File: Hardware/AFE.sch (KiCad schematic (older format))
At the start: 43 parts, among them U5 4069, U801 MCP47CXBX2, Y1 MountPad3, Y2 MountPad3

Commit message: Checking in some libraries.
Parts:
- removed GROUND1: GND_PAD, GaudiLabsFootPrints:MountPad3, symbol OpenThereminCC-rescue:TEST_1P
- removed W1: FIDUCIAL1, Fiducials:Fiducial_1mm_Dia_2.54mm_Outer_CopperTop, symbol OpenThereminCC-rescue:TEST_1P
- removed W2: FIDUCIAL2, Fiducials:Fiducial_1mm_Dia_2.54mm_Outer_CopperTop, symbol OpenThereminCC-rescue:TEST_1P
- removed Y1, Y2: MountPad3, GaudiLabsFootPrints:MountPad3, symbol OpenThereminCC-rescue:MountPad3
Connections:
- net labels added: PitchAnt, VolAnt
- wire segments 125 -> 123
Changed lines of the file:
@@
-$EndComp
-$Comp
-L OpenThereminCC-rescue:MountPad3 Y1
-U 1 1 5712BCA3
-P 850 1800
-F 0 "Y1" H 744 1600 60  0000 C CNN
-F 1 "MountPad3" H 900 1850 60  0000 C CNN
-F 2 "GaudiLabsFootPrints:MountPad3" H 850 1800 60  0001 C CNN
-F 3 "" H 850 1800 60  0000 C CNN
-	1    850  1800
-	-1   0    0    1
 $EndComp
 $Comp
@@
 $EndComp
 $Comp
-L OpenThereminCC-rescue:MountPad3 Y2
-U 1 1 571F63BE
-P 850 5250
-F 0 "Y2" H 744 5050 60  0000 C CNN
-F 1 "MountPad3" H 900 5300 60  0000 C CNN
-F 2 "GaudiLabsFootPrints:MountPad3" H 850 5250 60  0001 C CNN
-F 3 "" H 850 5250 60  0000 C CNN
-	1    850  5250
-	-1   0    0    1
-$EndComp
-$Comp
 L OpenThereminCC-rescue:FILTER L2
 U 1 1 571F63C6
@@
 	3650 4900 3650 4550
 Wire Wire Line
-	850  5250 850  4250
-Wire Wire Line
 	1700 7000 2200 7000
 Wire Wire Line
@@
 	1    0    0    -1
 $EndComp
-Wire Wire Line
-	850  1800 850  800
-$Comp
-L OpenThereminCC-rescue:TEST_1P GROUND1
-U 1 1 5735D84B
-P 3000 7100
-F 0 "GROUND1" H 2950 7250 50  0000 R CNN
-F 1 "GND_PAD" H 3100 7400 50  0000 R CNN
-F 2 "GaudiLabsFootPrints:MountPad3" H 3200 7100 50  0001 C CNN
-F 3 "" H 3200 7100 50  0000 C CNN
-	1    3000 7100
-	1    0    0    -1
-$EndComp
-$Comp
-L power:GND #PWR011
-U 1 1 5735ECC6
-P 3000 7100
-F 0 "#PWR011" H 3000 6850 50  0001 C CNN
-F 1 "GND" H 3008 6927 50  0000 C CNN
-F 2 "" H 3000 7100 50  0000 C CNN
-F 3 "" H 3000 7100 50  0000 C CNN
-	1    3000 7100
-	1    0    0    -1
-$EndComp
 $Comp
 L power:VSS #PWR017
@@
 	2300 2400 2300 2350
 Connection ~ 2550 2400
-$Comp
-L OpenThereminCC-rescue:TEST_1P W1
-U 1 1 57DB2880
-P 5900 7600
-F 0 "W1" V 5800 7650 50  0000 C CNN
-F 1 "FIDUCIAL1" V 5900 8000 50  0000 C CNN
-F 2 "Fiducials:Fiducial_1mm_Dia_2.54mm_Outer_CopperTop" H 6100 7600 50  0001 C CNN
-F 3 "" H 6100 7600 50  0000 C CNN
-	1    5900 7600
-	0    -1   -1   0
-$EndComp
-$Comp
-L OpenThereminCC-rescue:TEST_1P W2
-U 1 1 57DB3B8D
-P 6100 7600
-F 0 "W2" V 6200 7650 50  0000 L CNN
-F 1 "FIDUCIAL2" V 6100 7900 50  0000 L CNN
-F 2 "Fiducials:Fiducial_1mm_Dia_2.54mm_Outer_CopperTop" H 6300 7600 50  0001 C CNN
-F 3 "" H 6300 7600 50  0000 C CNN
-	1    6100 7600
-	0    1    1    0
-$EndComp
 Wire Wire Line
 	2550 1100 2750 1100
@@
 	1    0    0    -1
 $EndComp
+Text HLabel 900  1800 0    50   UnSpc ~ 0
+PitchAnt
+Text HLabel 900  5250 0    50   UnSpc ~ 0
+VolAnt
 $EndSCHEMATC

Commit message: Moving some components around.
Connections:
- net labels added: DAC_Latch, DO_PITCH, DO_VOLUME, i2c0_SCL, i2c0_SDA
- net labels removed: DAC_LATCH
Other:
- note added: "Changed DAC to i2c"
- note removed: "Change DAC to i2c"
- note removed: "TEST POINTS!!"
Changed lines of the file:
@@
 Wire Wire Line
 	1700 3550 2400 3550
-Text GLabel 8600 4600 2    60   Input ~ 0
-DAC_LATCH
 $Comp
 L OpenThereminCC-rescue:C C20
@@
 VO_VOL
 Text Notes 8150 6350 0    197  ~ 0
-Change DAC to i2c
-Text Notes 4250 5450 0    197  ~ 0
-TEST POINTS!!
-Text Notes 4300 1850 0    197  ~ 0
-TEST POINTS!!
+Changed DAC to i2c
 Text Notes 2400 5900 0    197  ~ 0
 220pF?\n
@@
 Text HLabel 900  5250 0    50   UnSpc ~ 0
 VolAnt
+Text HLabel 4450 1800 2    50   Output ~ 0
+DO_PITCH
+Text HLabel 4200 5250 2    50   Output ~ 0
+DO_VOLUME
+Text HLabel 8650 4200 2    50   BiDi ~ 0
+i2c0_SDA
+Text HLabel 8650 4300 2    50   Input ~ 0
+i2c0_SCL
+Text HLabel 8650 4600 2    50   Input ~ 0
+DAC_Latch
 $EndSCHEMATC

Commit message: Cleaning up a few associations, changing 0805 to 0603 footprints on AFE.
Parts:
- C801: renamed from C5; footprint GaudiLabsFootPrints:0805G -> Capacitor_SMD:C_0603_1608Metric_Pad1.08x0.95mm_HandSolder; symbol OpenThereminCC-rescue:C -> Device:C
- C802: renamed from C6; footprint GaudiLabsFootPrints:0805G -> Capacitor_SMD:C_0603_1608Metric_Pad1.08x0.95mm_HandSolder; symbol OpenThereminCC-rescue:C -> Device:C
- C803: renamed from C12; footprint GaudiLabsFootPrints:0805G -> Capacitor_SMD:C_0603_1608Metric_Pad1.08x0.95mm_HandSolder; symbol OpenThereminCC-rescue:C -> Device:C
- C804: renamed from C13; footprint GaudiLabsFootPrints:0805G -> Capacitor_SMD:C_0603_1608Metric_Pad1.08x0.95mm_HandSolder; symbol OpenThereminCC-rescue:C -> Device:C
- C805: renamed from C4; footprint GaudiLabsFootPrints:0805G -> Capacitor_SMD:C_0603_1608Metric_Pad1.08x0.95mm_HandSolder; symbol OpenThereminCC-rescue:C -> Device:C
- C806: renamed from C11; footprint GaudiLabsFootPrints:0805G -> Capacitor_SMD:C_0603_1608Metric_Pad1.08x0.95mm_HandSolder; symbol OpenThereminCC-rescue:C -> Device:C
- C807: renamed from C2; footprint GaudiLabsFootPrints:0805G -> Capacitor_SMD:C_0603_1608Metric_Pad1.08x0.95mm_HandSolder; symbol OpenThereminCC-rescue:C -> Device:C
- C808: renamed from C3; footprint GaudiLabsFootPrints:0805G -> Capacitor_SMD:C_0603_1608Metric_Pad1.08x0.95mm_HandSolder; symbol OpenThereminCC-rescue:C -> Device:C
- C809: renamed from C9; footprint GaudiLabsFootPrints:0805G -> Capacitor_SMD:C_0603_1608Metric_Pad1.08x0.95mm_HandSolder; symbol OpenThereminCC-rescue:C -> Device:C
- C810: renamed from C10; footprint GaudiLabsFootPrints:0805G -> Capacitor_SMD:C_0603_1608Metric_Pad1.08x0.95mm_HandSolder; symbol OpenThereminCC-rescue:C -> Device:C
- C811: renamed from C7; footprint GaudiLabsFootPrints:0805G -> Capacitor_SMD:C_0603_1608Metric_Pad1.08x0.95mm_HandSolder; symbol OpenThereminCC-rescue:C -> Device:C
- C812: renamed from C14; footprint GaudiLabsFootPrints:0805G -> Capacitor_SMD:C_0603_1608Metric_Pad1.08x0.95mm_HandSolder; symbol OpenThereminCC-rescue:C -> Device:C
- C813: renamed from C1; footprint GaudiLabsFootPrints:0805G -> Capacitor_SMD:C_0603_1608Metric_Pad1.08x0.95mm_HandSolder; symbol OpenThereminCC-rescue:C -> Device:C
- C814: renamed from C8; footprint GaudiLabsFootPrints:0805G -> Capacitor_SMD:C_0603_1608Metric_Pad1.08x0.95mm_HandSolder; symbol OpenThereminCC-rescue:C -> Device:C
- C815: renamed from C23; footprint GaudiLabsFootPrints:0805G -> Capacitor_SMD:C_0603_1608Metric_Pad1.08x0.95mm_HandSolder; symbol OpenThereminCC-rescue:C -> Device:C
- C816: renamed from C24; footprint GaudiLabsFootPrints:0805G -> Capacitor_SMD:C_0603_1608Metric_Pad1.08x0.95mm_HandSolder; symbol OpenThereminCC-rescue:C -> Device:C
- C817: renamed from C25; footprint GaudiLabsFootPrints:0805G -> Capacitor_SMD:C_0603_1608Metric_Pad1.08x0.95mm_HandSolder; symbol OpenThereminCC-rescue:C -> Device:C
- C818: renamed from C26; footprint GaudiLabsFootPrints:0805G -> Capacitor_SMD:C_0603_1608Metric_Pad1.08x0.95mm_HandSolder; symbol OpenThereminCC-rescue:C -> Device:C
- C819: renamed from C27; footprint GaudiLabsFootPrints:0805G -> Capacitor_SMD:C_0603_1608Metric_Pad1.08x0.95mm_HandSolder; symbol OpenThereminCC-rescue:C -> Device:C
- C820: renamed from C28; footprint GaudiLabsFootPrints:0805G -> Capacitor_SMD:C_0603_1608Metric_Pad1.08x0.95mm_HandSolder; symbol OpenThereminCC-rescue:C -> Device:C
- C821: renamed from C20; footprint GaudiLabsFootPrints:0805G -> Capacitor_SMD:C_0603_1608Metric_Pad1.08x0.95mm_HandSolder; symbol OpenThereminCC-rescue:C -> Device:C
- R801: renamed from R3; footprint GaudiLabsFootPrints:0805G -> Resistor_SMD:R_0603_1608Metric_Pad0.98x0.95mm_HandSolder
- R802: renamed from R7; footprint GaudiLabsFootPrints:0805G -> Resistor_SMD:R_0603_1608Metric_Pad0.98x0.95mm_HandSolder
- R803: renamed from R4; footprint GaudiLabsFootPrints:0805G -> Capacitor_SMD:C_0603_1608Metric_Pad1.08x0.95mm_HandSolder
- R804: renamed from R8; footprint GaudiLabsFootPrints:0805G -> Resistor_SMD:R_0603_1608Metric_Pad0.98x0.95mm_HandSolder
- R805: renamed from R1; footprint GaudiLabsFootPrints:0805G -> Resistor_SMD:R_0603_1608Metric_Pad0.98x0.95mm_HandSolder
- R806: renamed from R5; footprint GaudiLabsFootPrints:0805G -> Resistor_SMD:R_0603_1608Metric_Pad0.98x0.95mm_HandSolder
- R807: renamed from R2; footprint GaudiLabsFootPrints:0805G -> Resistor_SMD:R_0603_1608Metric_Pad0.98x0.95mm_HandSolder
- R808: renamed from R6; footprint GaudiLabsFootPrints:0805G -> Resistor_SMD:R_0603_1608Metric_Pad0.98x0.95mm_HandSolder
- R809: renamed from R15; footprint GaudiLabsFootPrints:0805G -> Resistor_SMD:R_0603_1608Metric_Pad0.98x0.95mm_HandSolder
- renumbered D1 to D801, D2 to D802, L1 to L801, L2 to L802, U5 to U801, U801 to U802

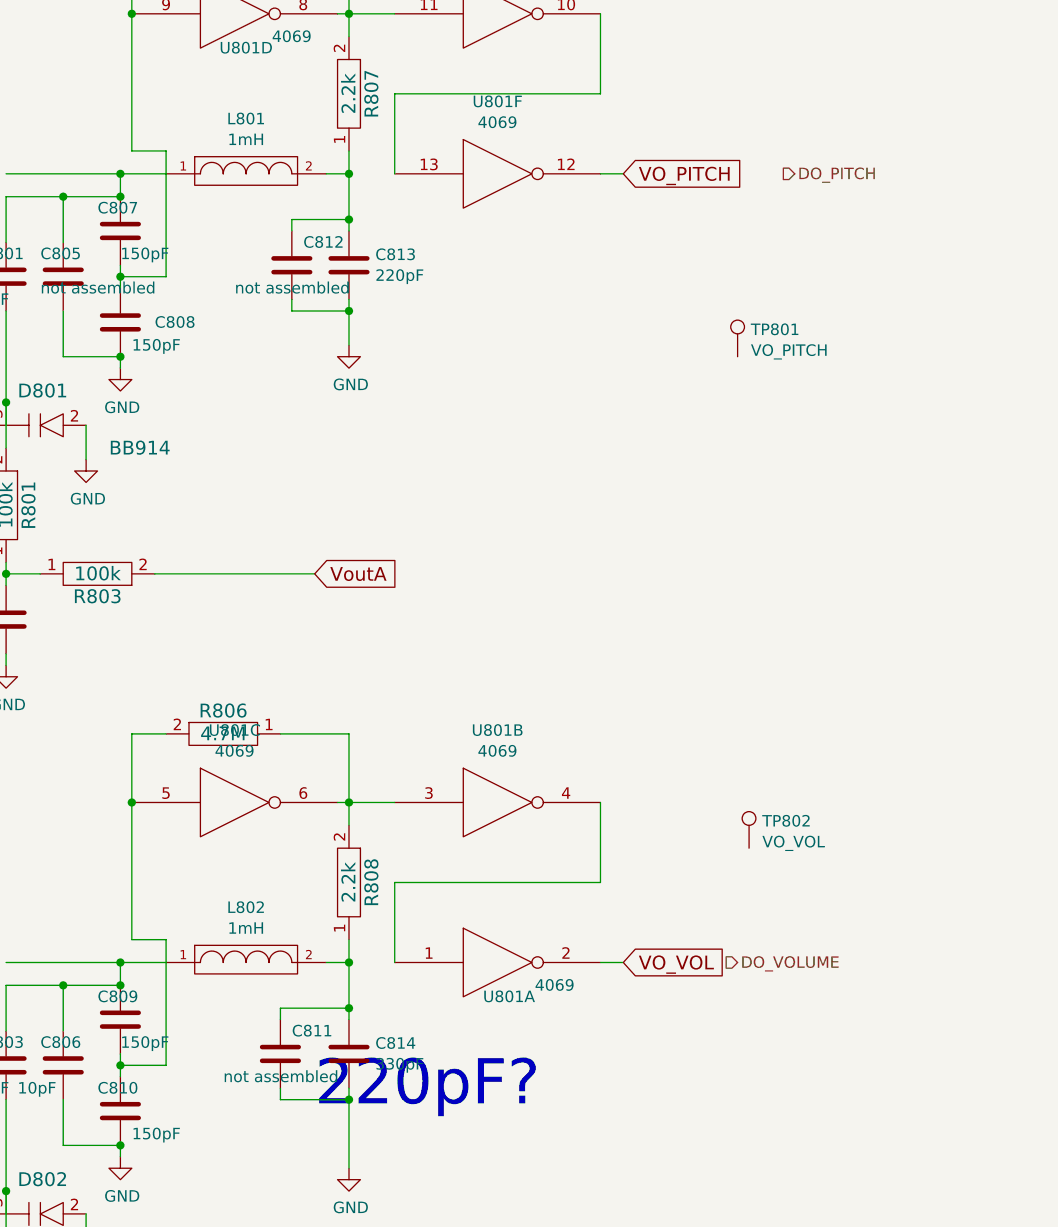
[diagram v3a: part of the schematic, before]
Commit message: Cleaning up some more, adding sourcing information.
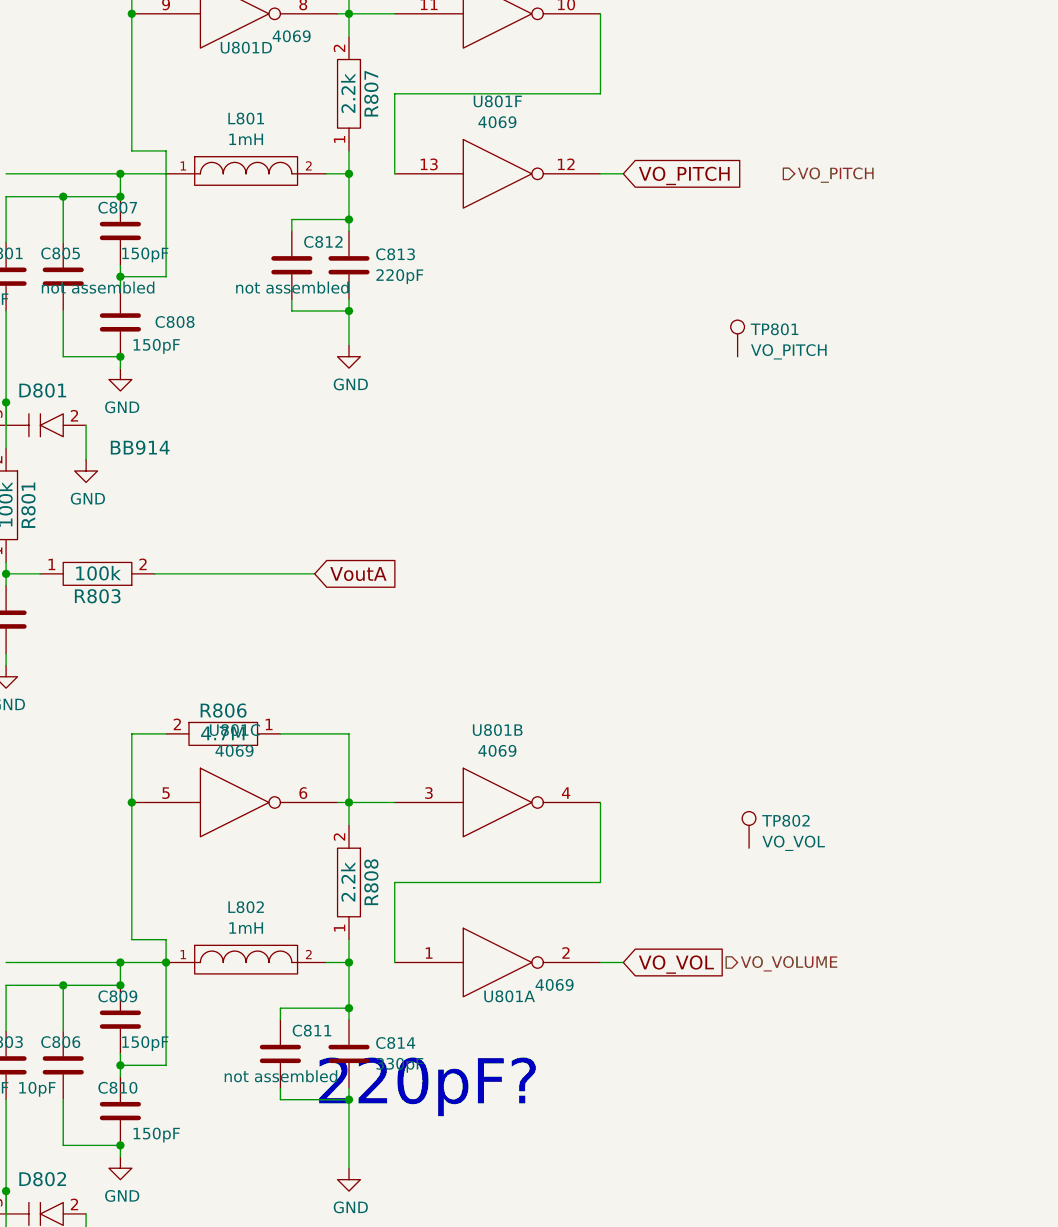
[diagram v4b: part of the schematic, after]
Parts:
- D801, D802: footprint TO_SOT_Packages_SMD:SOT-23 -> Package_TO_SOT_SMD:SOT-23; MPN (none) -> BB 914 E6327; MouserPN (none) -> 726-BB914E6327
- L801, L802: MPN (none) -> NL453232T-102J-PF; MouserPN (none) -> 810-NL453232T-102JPF
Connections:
- net at C809.2, C810.1, R806.2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: now also C803.1, C806.1, C809.1, L802.1
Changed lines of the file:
@@
 F 1 "1mH" H 2100 1949 50  0000 C CNN
 F 2 "GaudiLabsFootPrints:COIL" H 2100 1800 50  0001 C CNN
-F 3 "" H 2100 1800 50  0000 C CNN
+F 3 "https://product.tdk.com/system/files/dam/doc/product/inductor/inductor/smd/catalog/inductor_commercial_standard_nl453232_en.pdf" H 2100 1800 50  0001 C CNN
+F 4 "NL453232T-102J-PF " H 2100 1800 50  0001 C CNN "MPN"
+F 5 "810-NL453232T-102JPF" H 2100 1800 50  0001 C CNN "MouserPN"
 	1    2100 1800
 	1    0    0    -1
@@
 F 0 "D801" H 1100 3050 60  0000 L CNN
 F 1 "BB914" H 1500 2800 60  0000 L CNN
-F 2 "TO_SOT_Packages_SMD:SOT-23" H 1050 2900 60  0001 C CNN
-F 3 "" H 1050 2900 60  0000 C CNN
+F 2 "Package_TO_SOT_SMD:SOT-23" H 1050 2900 60  0001 C CNN
+F 3 "https://au.mouser.com/datasheet/2/196/bb914series-84756.pdf" H 1050 2900 60  0001 C CNN
+F 4 "BB 914 E6327 " H 1050 2900 50  0001 C CNN "MPN"
+F 5 "726-BB914E6327 " H 1050 2900 50  0001 C CNN "MouserPN"
 	1    1050 2900
 	1    0    0    -1
@@
 $EndComp
 $Comp
-L OpenThereminCC-rescue:FILTER L802
-U 1 1 571F63C6
-P 2100 5250
-F 0 "L802" H 2100 5490 50  0000 C CNN
-F 1 "1mH" H 2100 5399 50  0000 C CNN
-F 2 "GaudiLabsFootPrints:COIL" H 2100 5250 50  0001 C CNN
-F 3 "" H 2100 5250 50  0000 C CNN
-	1    2100 5250
-	1    0    0    -1
-$EndComp
-$Comp
 L OpenThereminCC-rescue:RES R806
 U 1 1 571F63D2
@@
 $EndComp
 $Comp
-L OpenThereminCC-rescue:CapDiode D802
-U 1 1 571F6429
-P 1050 6350
-F 0 "D802" H 1100 6500 60  0000 L CNN
-F 1 "BB914" H 1500 6250 60  0000 L CNN
-F 2 "TO_SOT_Packages_SMD:SOT-23" H 1050 6350 60  0001 C CNN
-F 3 "" H 1050 6350 60  0000 C CNN
-	1    1050 6350
-	1    0    0    -1
-$EndComp
-$Comp
 L power:GND #PWR0806
 U 1 1 571F642F
@@
 	2550 4250 2550 4550
 Wire Wire Line
-	1750 5700 1750 5150
+	1750 5700 1750 5250
 Wire Wire Line
 	1750 5150 1600 5150
 Wire Wire Line
 	1550 6050 1550 6100
-Wire Wire Line
-	1050 5850 1050 6250
-Connection ~ 1050 6250
 Wire Wire Line
 	3650 4900 3650 4550
@@
 Wire Wire Line
 	1050 7000 1050 7050
-Wire Wire Line
-	1050 6250 1050 6450
 Wire Wire Line
 	3350 7250 3350 7300
@@
 VolAnt
 Text HLabel 4450 1800 2    50   Output ~ 0
-DO_PITCH
+VO_PITCH
 Text HLabel 4200 5250 2    50   Output ~ 0
-DO_VOLUME
+VO_VOLUME
 Text HLabel 8650 4200 2    50   BiDi ~ 0
 i2c0_SDA
@@
 	0    1    1    0
 $EndComp
+Wire Wire Line
+	1050 5850 1050 6250
+$Comp
+L OpenThereminCC-rescue:CapDiode D802
+U 1 1 612D4FD1
+P 1050 6350
+F 0 "D802" H 1100 6500 60  0000 L CNN
+F 1 "BB914" H 1500 6250 60  0000 L CNN
+F 2 "Package_TO_SOT_SMD:SOT-23" H 1050 6350 60  0001 C CNN
+F 3 "https://au.mouser.com/datasheet/2/196/bb914series-84756.pdf" H 1050 6350 60  0001 C CNN
+F 4 "BB 914 E6327 " H 1050 6350 50  0001 C CNN "MPN"
+F 5 "726-BB914E6327 " H 1050 6350 50  0001 C CNN "MouserPN"
+	1    1050 6350
+	1    0    0    -1
+$EndComp
+Connection ~ 1050 6250
+Wire Wire Line
+	1050 6250 1050 6450
+$Comp
+L OpenThereminCC-rescue:FILTER L802
+U 1 1 612DCEBA
+P 2100 5250
+F 0 "L802" H 2100 5490 50  0000 C CNN
+F 1 "1mH" H 2100 5399 50  0000 C CNN
+F 2 "GaudiLabsFootPrints:COIL" H 2100 5250 50  0001 C CNN
+F 3 "https://product.tdk.com/system/files/dam/doc/product/inductor/inductor/smd/catalog/inductor_commercial_standard_nl453232_en.pdf" H 2100 5250 50  0001 C CNN
+F 4 "NL453232T-102J-PF " H 2100 5250 50  0001 C CNN "MPN"
+F 5 "810-NL453232T-102JPF" H 2100 5250 50  0001 C CNN "MouserPN"
+	1    2100 5250
+	1    0    0    -1
+$EndComp
+Connection ~ 1750 5250
+Wire Wire Line
+	1750 5250 1750 5150
 $EndSCHEMATC

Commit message: Updating 4069 device to TSSOP14 package.
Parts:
- L801, L802: footprint GaudiLabsFootPrints:COIL -> OHMC2022:IND.1812.NL453232T
- U801: footprint GaudiLabsFootPrints:SOIC-14_N -> OHMC2022:TSSOP14; symbol OpenThereminCC-rescue:4069 -> OHMC2022:4069.HEF4069UBTT,118; DPN (none) -> 1727-6749-1-ND; MPN (none) -> HEF4069UBTT,118
- U801: footprint GaudiLabsFootPrints:SOIC-14_N -> OHMC2022:TSSOP14; symbol OpenThereminCC-rescue:4069 -> OHMC2022:4069.HEF4069UBTT,118
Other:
- note added: "Changed 4069 PKG."
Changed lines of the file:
@@
 $EndDescr
 $Comp
-L OpenThereminCC-rescue:4069 U801
+L OHMC2022:4069.HEF4069UBTT,118 U801
 U 2 1 570FE1BD
 P 3200 4550
 F 0 "U801" H 3200 4865 50  0000 C CNN
 F 1 "4069" H 3200 4774 50  0000 C CNN
-F 2 "GaudiLabsFootPrints:SOIC-14_N" H 3200 4550 60  0001 C CNN
-F 3 "" H 3200 4550 60  0000 C CNN
+F 2 "OHMC2022:TSSOP14" H 3200 4550 60  0001 C CNN
+F 3 "https://assets.nexperia.com/documents/data-sheet/HEF4069UB.pdf" H 3200 4550 60  0001 C CNN
 	2    3200 4550
 	1    0    0    -1
 $EndComp
 $Comp
-L OpenThereminCC-rescue:4069 U801
+L OHMC2022:4069.HEF4069UBTT,118 U801
 U 3 1 570FE343
 P 2050 4550
 F 0 "U801" H 2050 4865 50  0000 C CNN
 F 1 "4069" H 2050 4774 50  0000 C CNN
-F 2 "GaudiLabsFootPrints:SOIC-14_N" H 2050 4550 60  0001 C CNN
-F 3 "" H 2050 4550 60  0000 C CNN
+F 2 "OHMC2022:TSSOP14" H 2050 4550 60  0001 C CNN
+F 3 "https://assets.nexperia.com/documents/data-sheet/HEF4069UB.pdf" H 2050 4550 60  0001 C CNN
 	3    2050 4550
 	1    0    0    -1
@@
 F 0 "L801" H 2100 2040 50  0000 C CNN
 F 1 "1mH" H 2100 1949 50  0000 C CNN
-F 2 "GaudiLabsFootPrints:COIL" H 2100 1800 50  0001 C CNN
+F 2 "OHMC2022:IND.1812.NL453232T" H 2100 1800 50  0001 C CNN
 F 3 "https://product.tdk.com/system/files/dam/doc/product/inductor/inductor/smd/catalog/inductor_commercial_standard_nl453232_en.pdf" H 2100 1800 50  0001 C CNN
 F 4 "NL453232T-102J-PF " H 2100 1800 50  0001 C CNN "MPN"
@@
 $EndComp
 $Comp
-L OpenThereminCC-rescue:4069 U801
+L OHMC2022:4069.HEF4069UBTT,118 U801
 U 1 1 570FE0DB
 P 3200 5250
 F 0 "U801" H 3250 5100 50  0000 C CNN
 F 1 "4069" H 3450 5150 50  0000 C CNN
-F 2 "GaudiLabsFootPrints:SOIC-14_N" H 3200 5250 60  0001 C CNN
-F 3 "" H 3200 5250 60  0000 C CNN
+F 2 "OHMC2022:TSSOP14" H 3200 5250 60  0001 C CNN
+F 3 "https://assets.nexperia.com/documents/data-sheet/HEF4069UB.pdf" H 3200 5250 60  0001 C CNN
+F 4 "1727-6749-1-ND" H 3200 5250 50  0001 C CNN "DPN"
+F 5 "HEF4069UBTT,118" H 3200 5250 50  0001 C CNN "MPN"
 	1    3200 5250
 	1    0    0    -1
@@
 $EndComp
 $Comp
-L OpenThereminCC-rescue:4069 U801
+L OHMC2022:4069.HEF4069UBTT,118 U801
 U 5 1 571F63B2
 P 3200 1100
 F 0 "U801" H 3200 1415 50  0000 C CNN
 F 1 "4069" H 3200 1324 50  0000 C CNN
-F 2 "GaudiLabsFootPrints:SOIC-14_N" H 3200 1100 60  0001 C CNN
-F 3 "" H 3200 1100 60  0000 C CNN
+F 2 "OHMC2022:TSSOP14" H 3200 1100 60  0001 C CNN
+F 3 "https://assets.nexperia.com/documents/data-sheet/HEF4069UB.pdf" H 3200 1100 60  0001 C CNN
 	5    3200 1100
 	1    0    0    -1
 $EndComp
 $Comp
-L OpenThereminCC-rescue:4069 U801
+L OHMC2022:4069.HEF4069UBTT,118 U801
 U 6 1 571F63B8
 P 3200 1800
 F 0 "U801" H 3200 2115 50  0000 C CNN
 F 1 "4069" H 3200 2024 50  0000 C CNN
-F 2 "GaudiLabsFootPrints:SOIC-14_N" H 3200 1800 60  0001 C CNN
-F 3 "" H 3200 1800 60  0000 C CNN
+F 2 "OHMC2022:TSSOP14" H 3200 1800 60  0001 C CNN
+F 3 "https://assets.nexperia.com/documents/data-sheet/HEF4069UB.pdf" H 3200 1800 60  0001 C CNN
 	6    3200 1800
 	1    0    0    -1
@@
 $EndComp
 $Comp
-L OpenThereminCC-rescue:4069 U801
+L OHMC2022:4069.HEF4069UBTT,118 U801
 U 4 1 571F63F6
 P 2050 1100
 F 0 "U801" H 2100 950 50  0000 C CNN
 F 1 "4069" H 2300 1000 50  0000 C CNN
-F 2 "GaudiLabsFootPrints:SOIC-14_N" H 2050 1100 60  0001 C CNN
-F 3 "" H 2050 1100 60  0000 C CNN
+F 2 "OHMC2022:TSSOP14" H 2050 1100 60  0001 C CNN
+F 3 "https://assets.nexperia.com/documents/data-sheet/HEF4069UB.pdf" H 2050 1100 60  0001 C CNN
 	4    2050 1100
 	1    0    0    -1
@@
 F 0 "L802" H 2100 5490 50  0000 C CNN
 F 1 "1mH" H 2100 5399 50  0000 C CNN
-F 2 "GaudiLabsFootPrints:COIL" H 2100 5250 50  0001 C CNN
+F 2 "OHMC2022:IND.1812.NL453232T" H 2100 5250 50  0001 C CNN
 F 3 "https://product.tdk.com/system/files/dam/doc/product/inductor/inductor/smd/catalog/inductor_commercial_standard_nl453232_en.pdf" H 2100 5250 50  0001 C CNN
 F 4 "NL453232T-102J-PF " H 2100 5250 50  0001 C CNN "MPN"
@@
 Wire Wire Line
 	1750 5250 1750 5150
+Text Notes 8150 6000 0    197  ~ 0
+Changed 4069 PKG.
 $EndSCHEMATC
